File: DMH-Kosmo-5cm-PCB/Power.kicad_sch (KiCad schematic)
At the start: 14 parts, among them J0 Conn_01x01, J100 IDC_02x05, J101 IDC_02x08

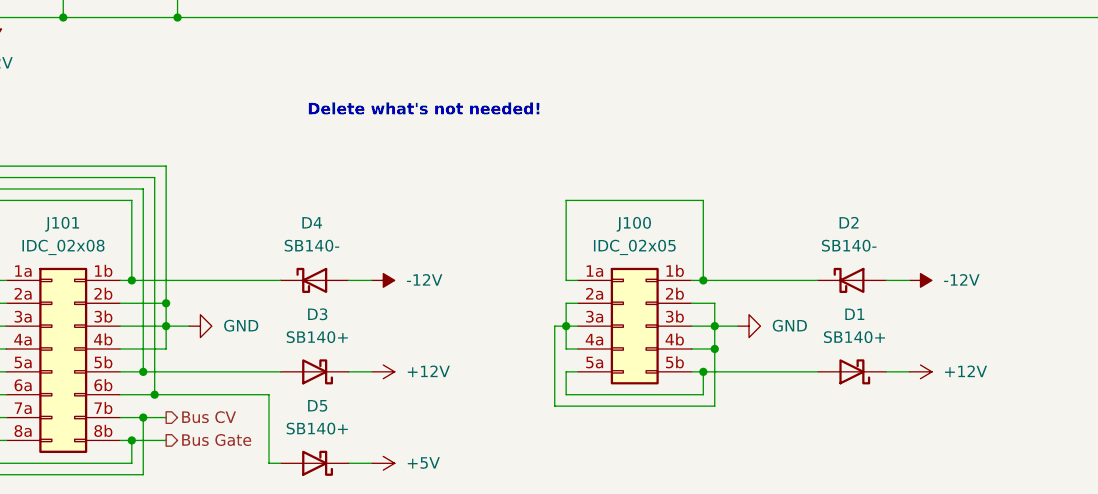
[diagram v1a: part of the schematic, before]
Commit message: Fixed schotky diodes
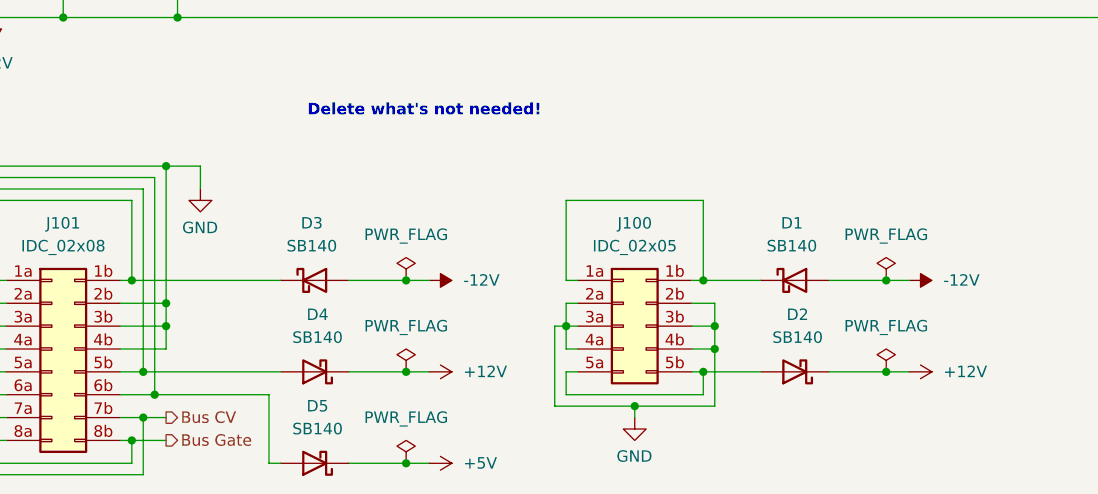
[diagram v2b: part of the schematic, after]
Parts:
- removed D1, D3, D5: SB140+, Diode_THT:D_DO-41_SOD81_P10.16mm_Horizontal, symbol SynthStuff:Power_Bus_Schotty_+
- removed D2, D4: SB140-, Diode_THT:D_DO-41_SOD81_P10.16mm_Horizontal, symbol SynthStuff:Power_Bus_Schotty_-
- added D1, D2, D3, D4, D5: SB140, Diode_THT:D_DO-41_SOD81_P10.16mm_Horizontal, symbol Diode:SB140
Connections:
- net +12V: now also D2.1 (K), D4.1 (K)
- net +5V: now also D5.1 (K)
- net -12V: now also D1.2 (A), D3.2 (A)
- net at J100.1a (Pin_1a), J100.1b (Pin_1b): now also D1.1 (K)
- net at J100.5a (Pin_5a), J100.5b (Pin_5b): now also D2.2 (A)
- net at J101.1a (Pin_1a), J101.1b (Pin_1b): now also D3.1 (K)
- net at J101.5a (Pin_5a), J101.5b (Pin_5b): now also D4.2 (A)
- net at J101.6a (Pin_6a), J101.6b (Pin_6b): now also D5.2 (A)
